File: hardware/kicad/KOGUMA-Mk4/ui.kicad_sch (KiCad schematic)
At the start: 23 parts, among them J7 DEBUG (STLINK-V3MODS), Q90 2N7002, SW2 TVAF06-A020B-R

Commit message: PB3 を前の LED に(D98 + R99 1kΩ、LED_FRONT)。46本すべて使う
回路図(MCU・表示のシート)、pinmap、check_pins、基板の参考の LED 位置 (35.2, 0)、部品表を更新。
基板の LED は回路図に合わせて 0603 として描く

Co-Authored-By: Claude Opus 5.5 <noreply@anthropic.com>
Claude-Session: https://claude.ai/code/session_01H2Zvpqxqu2v63zaiCMmfT3
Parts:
- added D98: FRONT, LED_SMD:LED_0603_1608Metric, symbol Device:LED
- added R99: 1k, Resistor_SMD:R_0603_1608Metric, symbol Device:R
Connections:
- net GND: now also D98.1 (K)
- new net: D98.2 (A), R99.2
- new net LED_FRONT: R99.1
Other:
- note added: "LED: GPIO が H で点灯(MK3 と同じ)。1kΩ で 約1mA(3.3V、LED の電圧降下 約2V)。モード3ビット + ナンバー4ビット + 前の LED(D98、PB3、2026-10-31)。電源の LED は電源のシート。"
- note removed: "LED: GPIO が H で点灯(MK3 と同じ)。1kΩ で 約1mA(3.3V、LED の電圧降下 約2V)。モード3ビット + ナンバー4ビット。電源の LED は電源のシート。"

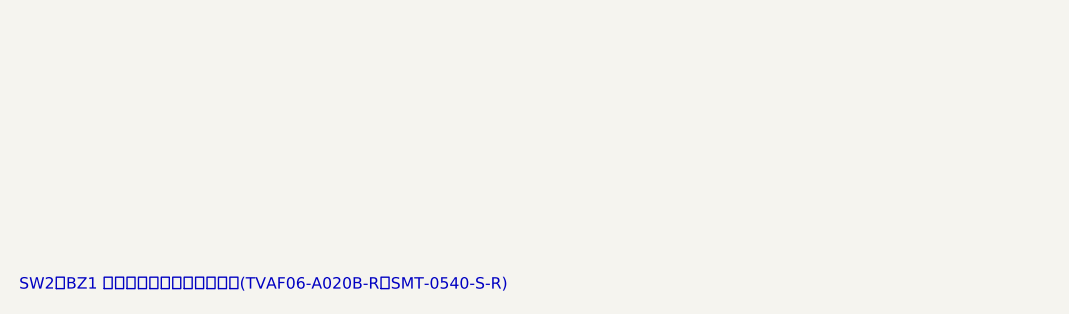
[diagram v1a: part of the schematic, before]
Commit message: SW1・SW2・BZ1 のフットプリントを作り、NJU6080 を SOT-23-6 に。全部の部品にフットプリントが付いた
寸法はメーカーの推奨ランド: SSSS810701(Alps の Land Dimensions)、TVAF06-A020B-R(仕様書の
P.C.B LAND DIMENSION)、SMT-0540-S-R(Suggested Land Pattern)。gen_footprints.py で作る。ERC エラー 0

Co-Authored-By: Claude Opus 5.5 <noreply@anthropic.com>
Claude-Session: https://claude.ai/code/session_01H2Zvpqxqu2v63zaiCMmfT3
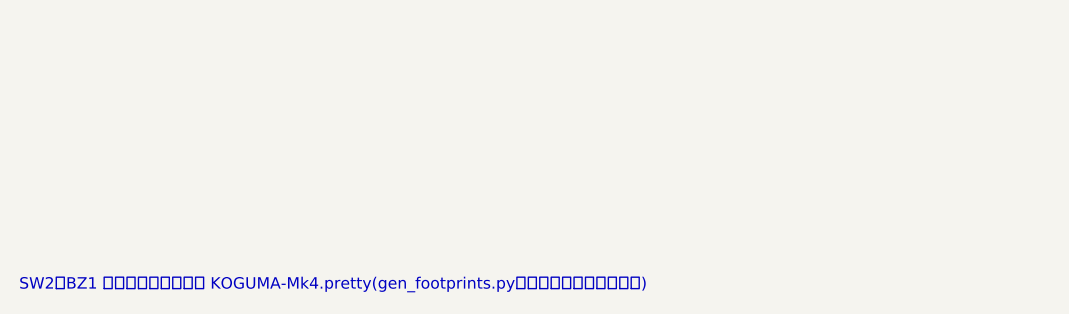
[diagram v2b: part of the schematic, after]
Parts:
- BZ1: footprint (none) -> KOGUMA-Mk4:Buzzer_PUI_SMT-0540
- SW2: footprint (none) -> KOGUMA-Mk4:SW_Push_Jianfu_TVAF06
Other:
- note added: "SW2・BZ1 のフットプリントは KOGUMA-Mk4.pretty(gen_footprints.py、メーカーの推奨ランド)"
- note removed: "SW2・BZ1 のフットプリントは未作成(TVAF06-A020B-R、SMT-0540-S-R)"
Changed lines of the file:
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@@
 			)
 		)
-		(property "Footprint" ""
+		(property "Footprint" "KOGUMA-Mk4:Buzzer_PUI_SMT-0540"
 			(at 147.32 60.96 0)
 			(effects
@@
 			)
 		)
-		(property "Footprint" ""
+		(property "Footprint" "KOGUMA-Mk4:SW_Push_Jianfu_TVAF06"
 			(at 208.28 63.5 90)
 			(effects
@@
 		)
 	)
-	(text "SW2・BZ1 のフットプリントは未作成(TVAF06-A020B-R、SMT-0540-S-R)"
+	(text "SW2・BZ1 のフットプリントは KOGUMA-Mk4.pretty(gen_footprints.py、メーカーの推奨ランド)"
 		(exclude_from_sim no)
 		(at 25.4 190.5 0)
